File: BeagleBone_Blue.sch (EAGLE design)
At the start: 413 parts, among them J1 68000-406HLF, M1 JST_ZH_2, M2 JST_ZH_2, M3 JST_ZH_2, M4 JST_ZH_2, P2 CTIJTAG, P3 87520-0010BLF, P4 UX60SC-MB-5ST(80), Q3 MOSFET-N, U1 MPU-9250, U10 TPD4S012, U12 MT41K256M16HA, U13 MTFC4GLDEA, U15 SN74LVC2G241DCU, U16 SN74LVC1G07DCK, U3 SN74LVC1G06DCK, U4 TL5209, U5 AM3358_BZCZ_324, U6 SN74LVC1G74_DCT_8, U7 24LC_32AT-I/OT, U8 TPS2051BD, U9 TPD4S012, Y1 CM200C-32.768KAZF-UT, Y2 445C33D24M00000, Y4 ASDMB-24.576MHZ-LC-T

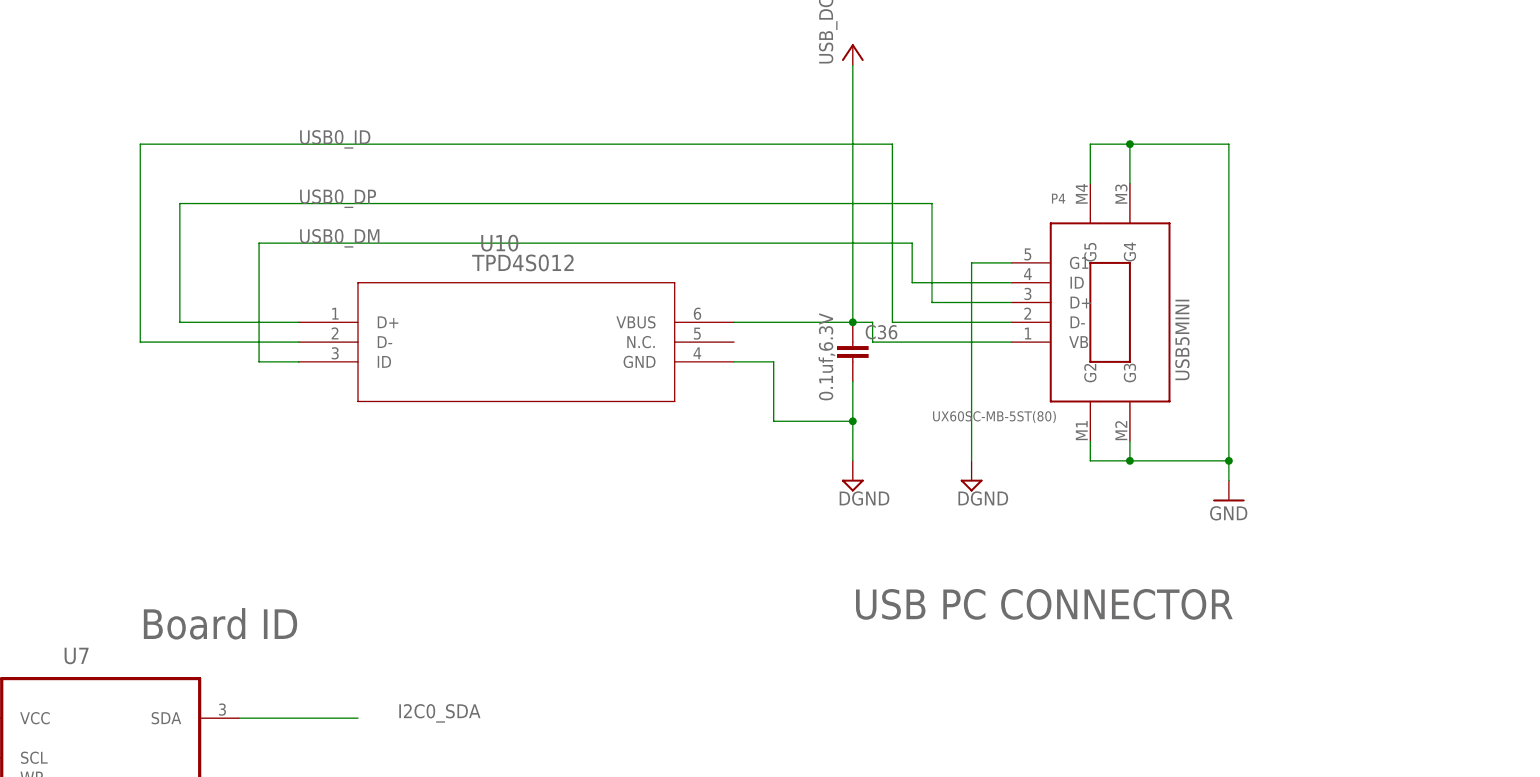
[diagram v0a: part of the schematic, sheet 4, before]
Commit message: swap mini usb for micro usb
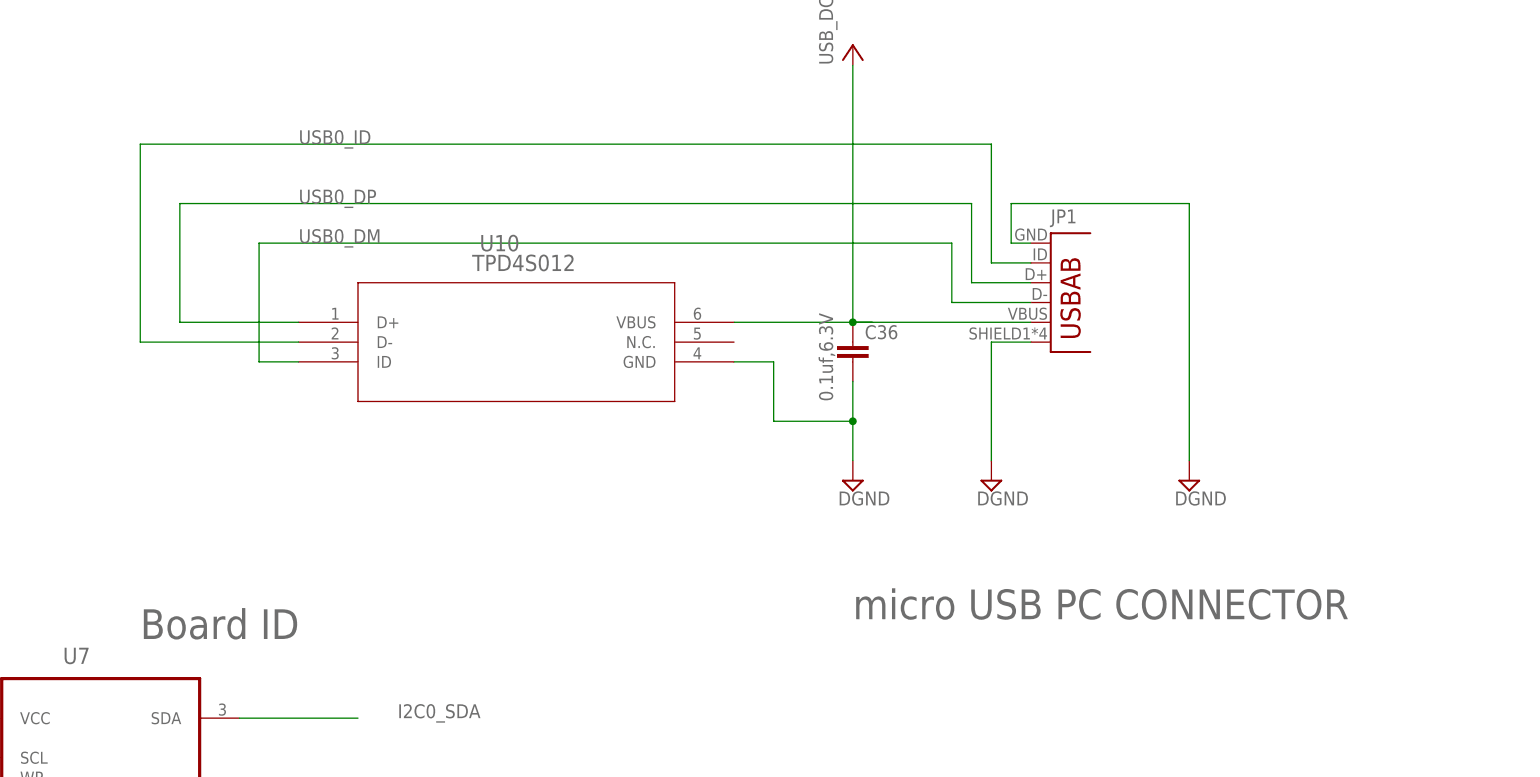
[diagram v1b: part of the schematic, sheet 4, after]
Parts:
- removed P4: UX60SC-MB-5ST(80), UX60SC-MB-5ST(80):UX60SC-MB-5ST(80)
- added JP1: (no value), Strawson_Eagle_Lib:USB-AB
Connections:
- net GND: now also JP1.GND, JP1.SHIELD; no longer P4.G1, P4.G2, P4.G3, P4.G4, P4.G5
- net N$255: now also JP1.D-; no longer P4.ID
- net N$256: now also JP1.D+; no longer P4.D+
- net N$257: now also JP1.USBID; no longer P4.D-
- net VCC: now also JP1.VBUS; no longer P4.VB
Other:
- note added: "micro USB PC CONNECTOR"
- note removed: "USB PC CONNECTOR"
- note removed: "USB5MINI"

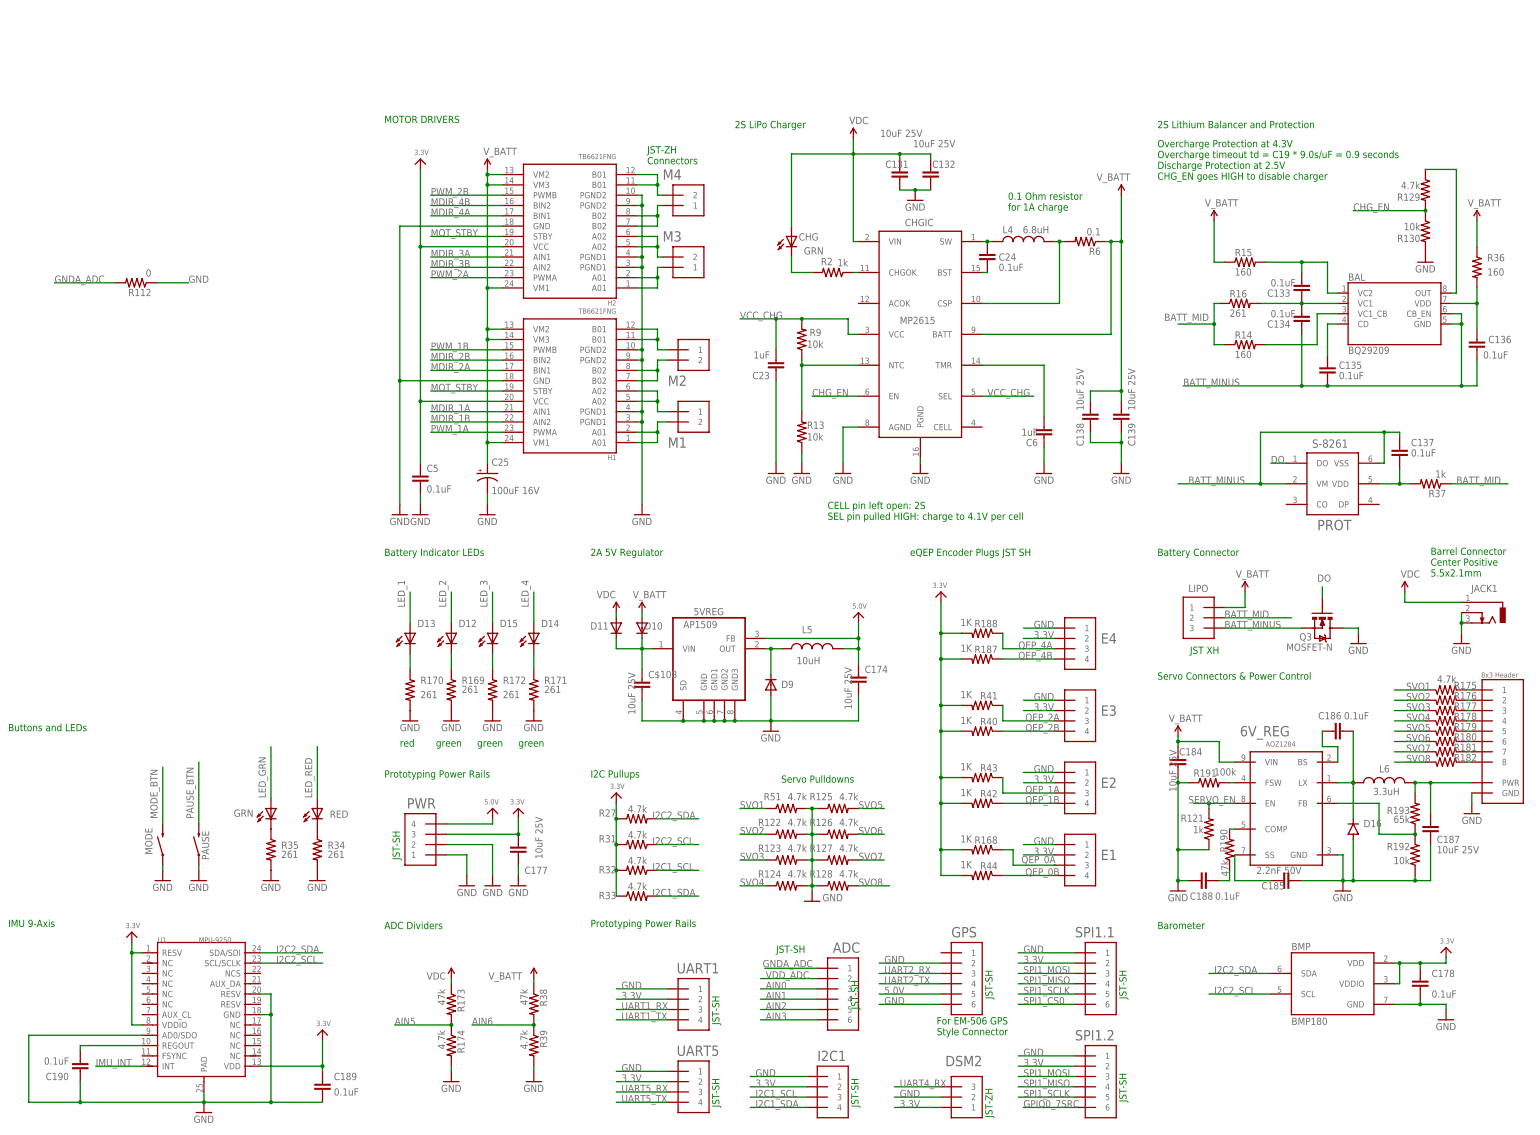
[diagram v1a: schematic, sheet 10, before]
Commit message: delete old single cell lipo connectors
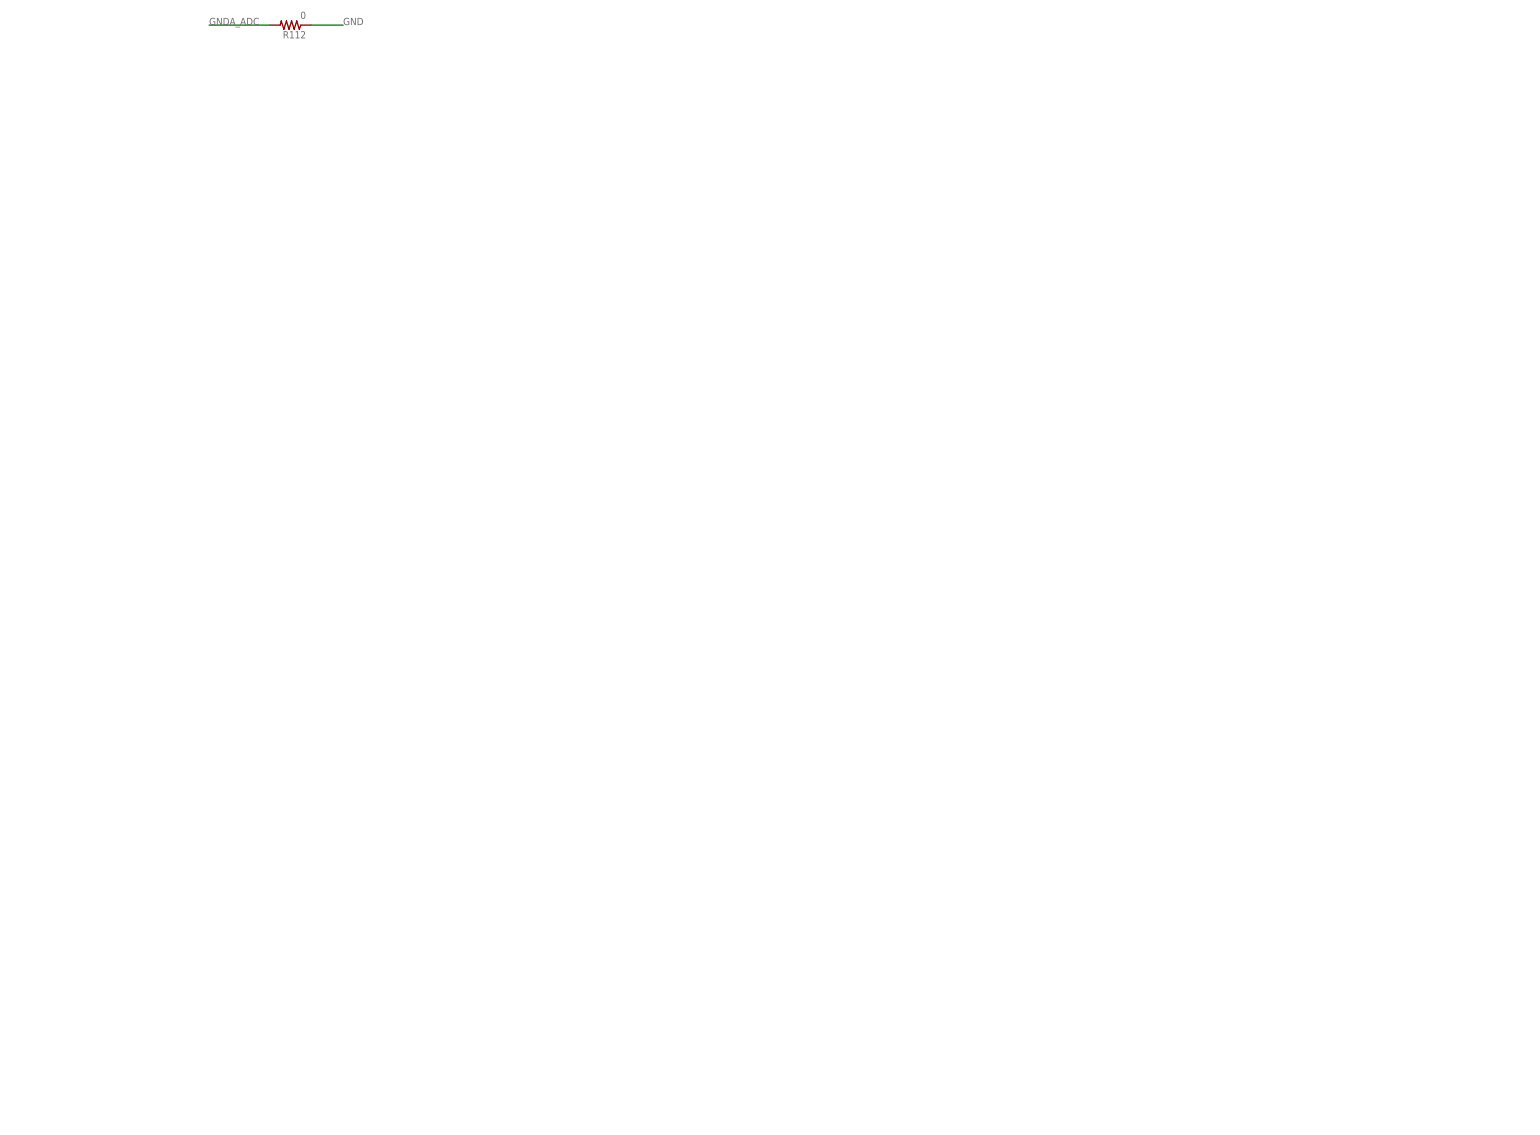
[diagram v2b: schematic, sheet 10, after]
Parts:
- removed 5VREG: AP1509SOIC-8-TIGHT, Strawson_Eagle_Lib:AP1509SOIC-8-TIGHT
- removed 6V_REG: AOZ1284, Strawson_Eagle_Lib:AOZ1284
- removed ADC, GPS, SPI1.1, SPI1.2: JST_SH_6, Strawson_Eagle_Lib:JST_SH_6
- removed BAL: BQ29209, Strawson_Eagle_Lib:BQ29209
- removed BMP: BMP180, SparkFun-Sensors:BMP180
- removed C$108, C131, C132, C138, C139, C174, C177, C184, C187: 10uF 25V, SparkFun-Capacitors:CAP0805
- removed C133, C134, C135, C136, C137, C178, C186, C188, C189, C190, C24, C5: 0.1uF, Strawson_Eagle_Lib:CAP0402-CAP
- removed C185: 2.2nF 50V, Strawson_Eagle_Lib:CAP0402-CAP
- removed C23, C6: 1uF, Strawson_Eagle_Lib:CAP0402-CAP
- removed C25: 100uF 16V, adafruit:CPOL-USD
- removed CHG, GRN: GRN, SparkFun-LED:LED0603
- removed CHGIC: MP2615, Strawson_Eagle_Lib:MP2615
- removed D10, D11, D9: (no value), adafruit:DIODESOD-123
- removed D12, D14, D15: GREEN, SparkFun-LED:LED0603
- removed D13, RED: RED, SparkFun-LED:LED0603
- removed D16: (no value), Strawson_Eagle_Lib:DIODEDO214AA
- removed DSM2: JST_ZH_3, Strawson_Eagle_Lib:JST_ZH_3
- removed E1, E2, E3, E4, I2C1, PWR, UART1, UART5: JST_SH_4, Strawson_Eagle_Lib:JST_SH_4
- removed H1, H2: TB6621FNG, SparkFun:TB6621FNG
- removed JACK1: 5.5x2.1mm, con-jack:DCJ0303
- removed L4: 6.8uH, SparkFun-Passives:INDUCTORBOURNS_SRN6045
- removed L5: 10uH, SparkFun-Passives:INDUCTORBOURNS_SRN6045
- removed L6: 3.3uH, Strawson_Eagle_Lib:INDUCTOR
- removed LIPO: (no value), Strawson_Eagle_Lib:JST_XH_3-PIN
- removed M1, M2, M3, M4: JST_ZH_2, Strawson_Eagle_Lib:JST_ZH_2
- removed MODE, PAUSE: SWITCH-MOMENTARY-2-SMD-1101NE, SparkFun-Electromechanical:SWITCH-MOMENTARY-2-SMD-1101NE
- removed PROT: S-8261, Strawson_Eagle_Lib:S-8261
- removed Q3: MOSFET-N, Strawson_Eagle_Lib:MOSFET-NCHANNEL
- removed R121, R2, R37: 1k, Strawson_Eagle_Lib:RESISTOR0402-RES
- removed R122, R123, R124, R125, R126, R127, R128, R129, R174, R175, R176, R177, R178, R179, R180, R181, R182, R27, R31, R32, R33, R39, R51: 4.7k, Strawson_Eagle_Lib:RESISTOR0402-RES
- removed R13, R130, R192, R9: 10k, Strawson_Eagle_Lib:RESISTOR0402-RES
- removed R14, R15, R36: 160, Strawson_Eagle_Lib:RESISTOR0402-RES
- removed R16, R169, R170, R171, R172, R34, R35: 261, Strawson_Eagle_Lib:RESISTOR0402-RES
- removed R168, R187, R188, R40, R41, R42, R43, R44: 1K, Strawson_Eagle_Lib:RESISTOR0402-RES
- removed R173, R190, R38: 47k, Strawson_Eagle_Lib:RESISTOR0402-RES
- removed R191: 100k, Strawson_Eagle_Lib:RESISTOR0402-RES
- removed R193: 65k, Strawson_Eagle_Lib:RESISTOR0402-RES
- removed R6: 0.1, SparkFun-Resistors:RESISTOR0603
- removed TP12, TP5, TP6, TP7, TP8: TESTPOINT, TESTPOINT:TESTPOINT
- removed U$14: SERVO_HEADERS_8X, Strawson_Eagle_Lib:SERVO_HEADERS_8X
- removed U1: MPU-9250, Strawson_Eagle_Lib:MPU-9250
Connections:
- removed net 3.3V: BMP.VDD, BMP.VDDIO, C177.1, C178.1, C189.1, C5.2, DSM2.1, E1.2, E2.2, E3.2, E4.2, H1.VCC, H2.VCC, I2C1.2, PWR.3, R168.2, R187.2, R188.2, R27.1, R31.2, R32.2, R33.1, R40.2, R41.2, R42.2, R43.2, R44.2, SPI1.1.2, SPI1.2.2, U1.RESV, U1.VDD, U1.VDDIO, UART1.2, UART5.2
- removed net 5.0V: 5VREG.FB, C174.1, GPS.5, L5.2, PWR.4
- removed net BATT_MID: LIPO.2, R14.1, R16.1, R37.1
- removed net BATT_MINUS: BAL.CB_EN, BAL.GND, C134.1, C135.2, C136.2, C137.1, LIPO.3, PROT.VM, PROT.VSS, Q3.S
- removed net CHG_EN: CHGIC.EN, R129.2, R130.1
- removed net CO: BAL.OUT, R129.1
- removed net DO: PROT.DO, Q3.G
- removed net L3: D15.C, R172.1
- removed net L4: D14.C, R171.1
- removed net MOT1A: H1.A01@1, H1.A01@2, M1.2
- removed net MOT1B: H1.A02@5, H1.A02@6, M1.1
- removed net MOT2A: H1.B01@11, H1.B01@12, M2.1
- removed net MOT2B: H1.B02@7, H1.B02@8, M2.2
- removed net MOT3A: H2.A01@1, H2.A01@2, M3.1
- removed net MOT3B: H2.A02@5, H2.A02@6, M3.2
- removed net MOT4A: H2.B01@11, H2.B01@12, M4.2
- removed net MOT4B: H2.B02@7, H2.B02@8, M4.1
- removed net N$10: U$3.BAT_SENSE
- removed net N$11: U$3.TS
- removed net N$12: R34.1, RED.C
- removed net N$13: C137.2, PROT.VDD, R37.2
- removed net N$14: C24.1, CHGIC.BST
- removed net N$15: GRN.C, R35.1
- removed net N$16: 5VREG.OUT, D9.C, L5.1
- removed net N$18: CHGIC.CHGOK, R2.1
- removed net N$20: R175.2, U$14.1
- removed net N$21: CHGIC.NTC, R13.2, R9.1
- removed net N$24: BAL.CD, C135.1
- removed net N$25: R176.2, U$14.2
- removed net N$29: BAL.VDD, C136.1, R36.2
- removed net N$30: R177.2, U$14.3
- removed net N$33: 6V_REG.SS, C185.2
- removed net N$38: R178.2, U$14.4
- removed net N$4: CHG.C, R2.2
- removed net N$48: D12.C, R169.1
- removed net N$49: D13.C, R170.1
- removed net N$5: U$3.BAT1, U$3.BAT2
- removed net N$50: BAL.VC1_CB, R14.2
- removed net N$51: R179.2, U$14.5
- removed net N$52: R180.2, U$14.6
- removed net N$53: 6V_REG.BS, C186.1
- removed net N$54: R181.2, U$14.7
- removed net N$55: C24.2, CHGIC.SW, L4.1
- removed net N$56: R182.2, U$14.8
- removed net N$6: BAL.VC1, C133.1, C134.2, R16.2
- removed net N$60: 6V_REG.LX, C186.2, D16.C, L6.1
- removed net N$61: 6V_REG.FSW, R191.2
- removed net N$62: C187.2, L6.2, R193.2, U$14.PWR
- removed net N$63: 6V_REG.COMP, R190.2
- removed net N$65: 6V_REG.FB, R192.2, R193.1
- removed net N$66: C188.2, R190.1
- removed net N$67: CHGIC.CSP, L4.2, R6.2
- removed net N$69: C6.2, CHGIC.TMR
- removed net N$7: BAL.VC2, C133.2, R15.2
- removed net N$70: C190.2, U1.REGOUT
- removed net N$79: 5VREG.VIN, C$108.1, D10.C, D11.C
- removed net VCC_CHG: C23.2, CHGIC.SEL, CHGIC.VCC, R9.2
- removed net VDD_ADC: ADC.2
- removed net V_BATT: 6V_REG.VIN, C138.1, C139.1, C184.2, C25.+, CHGIC.BATT, D10.A, H1.VM1, H1.VM2, H1.VM3, H2.VM1, H2.VM2, H2.VM3, LIPO.1, R15.1, R36.1, R38.1, R6.1
- net AIN0: no longer ADC.3
- net AIN1: no longer ADC.4
- net AIN2: no longer ADC.5
- net AIN3: no longer ADC.6
- net AIN5: no longer R173.2, R174.1
- net AIN6: no longer R38.2, R39.1
- net GND: no longer 5VREG.GND, 5VREG.GND1, 5VREG.GND2, 5VREG.GND3, 5VREG.SD, 6V_REG.GND, BMP.GND, C$108.2, C131.2, C132.2, C138.2, C139.2, C174.2, C177.2, C178.2, C184.1, C185.1, C187.1, C188.1, C189.2, C190.1, C23.1, C25.-, C5.1, C6.1, CHGIC.AGND, CHGIC.PGND, D16.A, D9.A, DSM2.2, E1.1, E2.1, E3.1, E4.1, GPS.2, GPS.6, H1.GND, H1.PGND1@3, H1.PGND1@4, H1.PGND2@10, H1.PGND2@9, H2.GND, H2.PGND1@3, H2.PGND1@4, H2.PGND2@10, H2.PGND2@9, I2C1.1, JACK1.2, JACK1.3, MODE.1, PAUSE.1, PWR.1, PWR.2, Q3.D, R121.1, R122.2, R123.2, R124.2, R125.1, R126.1, R127.1, R128.1, R13.1, R130.2, R169.2, R170.2, R171.2, R172.2, R174.2, R191.1, R192.1, R34.2, R35.2, R39.2, R51.2, SPI1.1.1, SPI1.2.1, U$14.GND, U1.AD0/SDO, U1.GND, U1.PAD, U1.RESV@2, UART1.1, UART5.1
- net GNDA_ADC: no longer ADC.1
- net GPIO0_7SRC: no longer SPI1.2.6
- net I2C1_SCL: no longer I2C1.3, R32.1
- net I2C1_SDA: no longer I2C1.4, R33.2
- net I2C2_SCL: no longer BMP.SCL, R31.1, U1.SCL/SCLK
- net I2C2_SDA: no longer BMP.SDA, R27.2, U1.SDA/SDI
- net IMU_INT: no longer U1.INT
- net LED_1: no longer D13.A
- net LED_2: no longer D12.A
- net LED_3: no longer D15.A
- net LED_4: no longer D14.A
- net LED_GRN: no longer GRN.A
- net LED_RED: no longer RED.A
- net MDIR_1A: no longer H1.AIN1
- net MDIR_1B: no longer H1.AIN2
- net MDIR_2A: no longer H1.BIN1
- net MDIR_2B: no longer H1.BIN2
- net MDIR_3A: no longer H2.AIN1
- net MDIR_3B: no longer H2.AIN2
- net MDIR_4A: no longer H2.BIN1
- net MDIR_4B: no longer H2.BIN2
- net MODE_BTN: no longer MODE.2
- net MOT_STBY: no longer H1.STBY, H2.STBY
- net PAUSE_BTN: no longer PAUSE.2
- net PWM_1A: no longer H1.PWMA
- net PWM_1B: no longer H1.PWMB
- net PWM_2A: no longer H2.PWMA
- net PWM_2B: no longer H2.PWMB
- net QEP_0A: no longer E1.3, R168.1
- net QEP_0B: no longer E1.4, R44.1
- net QEP_1A: no longer E2.3, R43.1
- net QEP_1B: no longer E2.4, R42.1
- net QEP_2A: no longer E3.3, R41.1
- net QEP_2B: no longer E3.4, R40.1
- net QEP_4A: no longer E4.3, R188.1
- net QEP_4B: no longer E4.4, R187.1
- net SERVO_EN: no longer 6V_REG.EN, R121.2
- net SPI1_CS0: no longer SPI1.1.6
- net SPI1_MISO: no longer SPI1.1.4, SPI1.2.4
- net SPI1_MOSI: no longer SPI1.1.3, SPI1.2.3
- net SPI1_SCLK: no longer SPI1.1.5, SPI1.2.5
- net SVO1: no longer R175.1, R51.1
- net SVO2: no longer R122.1, R176.1
- net SVO3: no longer R123.1, R177.1
- net SVO4: no longer R124.1, R178.1
- net SVO5: no longer R125.2, R179.1
- net SVO6: no longer R126.2, R180.1
- net SVO7: no longer R127.2, R181.1
- net SVO8: no longer R128.2, R182.1
- net UART1_RX: no longer UART1.3
- net UART1_TX: no longer UART1.4
- net UART2_RX: no longer GPS.3
- net UART2_TX: no longer GPS.4
- net UART4_RX: no longer DSM2.3
- net UART5_RX: no longer UART5.3
- net UART5_TX: no longer UART5.4
- net VCC: no longer C131.1, C132.1, CHG.A, CHGIC.VIN, D11.A, JACK1.1, R173.1
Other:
- note removed: "0.1 Ohm resistor for 1A charge"
- note removed: "2A 5V Regulator"
- note removed: "2S LiPo Charger"
- note removed: "2S Lithium Balancer and Protection"
- note removed: "ADC Dividers"
- note removed: "Barometer"
- note removed: "Barrel Connector Center Positive 5.5x2.1mm"
- note removed: "Battery Connector"
- note removed: "Battery Indicator LEDs"
- note removed: "Battery access pins. Pins are randomly placed to fit them in, but will be able to tie into them either with a cape or wires. Pins will not be populated."
- note removed: "Buttons and LEDs"
- note removed: "CELL pin left open: 2S SEL pin pulled HIGH: charge to 4.1V per cell"
- note removed: "For EM-506 GPS Style Connector"
- note removed: "I2C Pullups"
- note removed: "IMU 9-Axis"
- note removed: "JST XH"
- note removed: "JST-SH"
- note removed: "JST-ZH"
- note removed: "JST-ZH Connectors"
- note removed: "MOTOR DRIVERS"
- note removed: "Overcharge Protection at 4.3V Overcharge timeout td = C19 * 9.0s/uF = 0.9 seconds Discharge Protection at 2.5V CHG_EN goes HIGH to disable charger"
- note removed: "Prototyping Power Rails"
- note removed: "Servo Connectors & Power Control"
- note removed: "Servo Pulldowns"
- note removed: "eQEP Encoder Plugs JST SH"
- note removed: "green"
- note removed: "red"
- moved on the sheet: R112

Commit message: remove old 5V power connector
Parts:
- removed U$1: PJ-002A, PJ-002A:PJ-002A
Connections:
- net GND: no longer U$1.2
- net VCC: no longer U$1.1
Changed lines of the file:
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@@
 <part name="S3" library="KMR231GLFS" deviceset="KMR231GLFS" device=""/>
 <part name="SUPPLY108" library="supply2" deviceset="GND" device="" value="DGND"/>
-<part name="U$1" library="PJ-002A" deviceset="PJ-002A" device=""/>
-<part name="SUPPLY109" library="supply2" deviceset="GND" device="" value="DGND"/>
 <part name="L2" library="LQM2HPN2RMG0L" deviceset="LQM2HPN2RMG0L" device="" value=""/>
 <part name="L3" library="LQM2HPN2RMG0L" deviceset="LQM2HPN2RMG0L" device="" value=""/>
@@
 <instance part="S3" gate="G$1" x="20.32" y="7.62"/>
 <instance part="SUPPLY108" gate="GND" x="-22.86" y="-5.08"/>
-<instance part="U$1" gate="G$1" x="-38.1" y="73.66"/>
-<instance part="SUPPLY109" gate="GND" x="-27.94" y="63.5"/>
 <instance part="L2" gate="G$1" x="119.38" y="12.7" rot="R180"/>
 <instance part="L3" gate="G$1" x="119.38" y="2.54" rot="R180"/>
@@
 <pinref part="SUPPLY108" gate="GND" pin="GND"/>
 <junction x="-22.86" y="12.7"/>
-</segment>
-<segment>
-<pinref part="U$1" gate="G$1" pin="2"/>
-<wire x1="-20.32" y1="78.74" x2="-15.24" y2="78.74" width="0.1524" layer="91"/>
-<wire x1="-15.24" y1="78.74" x2="-15.24" y2="76.2" width="0.1524" layer="91"/>
-<wire x1="-15.24" y1="76.2" x2="-27.94" y2="76.2" width="0.1524" layer="91"/>
-<wire x1="-27.94" y1="76.2" x2="-27.94" y2="66.04" width="0.1524" layer="91"/>
-<pinref part="SUPPLY109" gate="GND" pin="GND"/>
 </segment>
 <segment>
@@
 <wire x1="66.04" y1="83.82" x2="5.08" y2="83.82" width="0.1524" layer="91"/>
 <junction x="5.08" y="83.82"/>
-<pinref part="U$1" gate="G$1" pin="1"/>
-<wire x1="-20.32" y1="83.82" x2="5.08" y2="83.82" width="0.1524" layer="91"/>
 <pinref part="U$3" gate="G$1" pin="AC"/>
 </segment>
